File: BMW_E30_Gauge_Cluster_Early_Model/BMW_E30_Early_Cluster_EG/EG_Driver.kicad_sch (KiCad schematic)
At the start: 23 parts, among them Q2 BC337, U1 4049, U4 LM2903, U5 SAJ300R, U6 PIC1655A, Y1 160 kHz

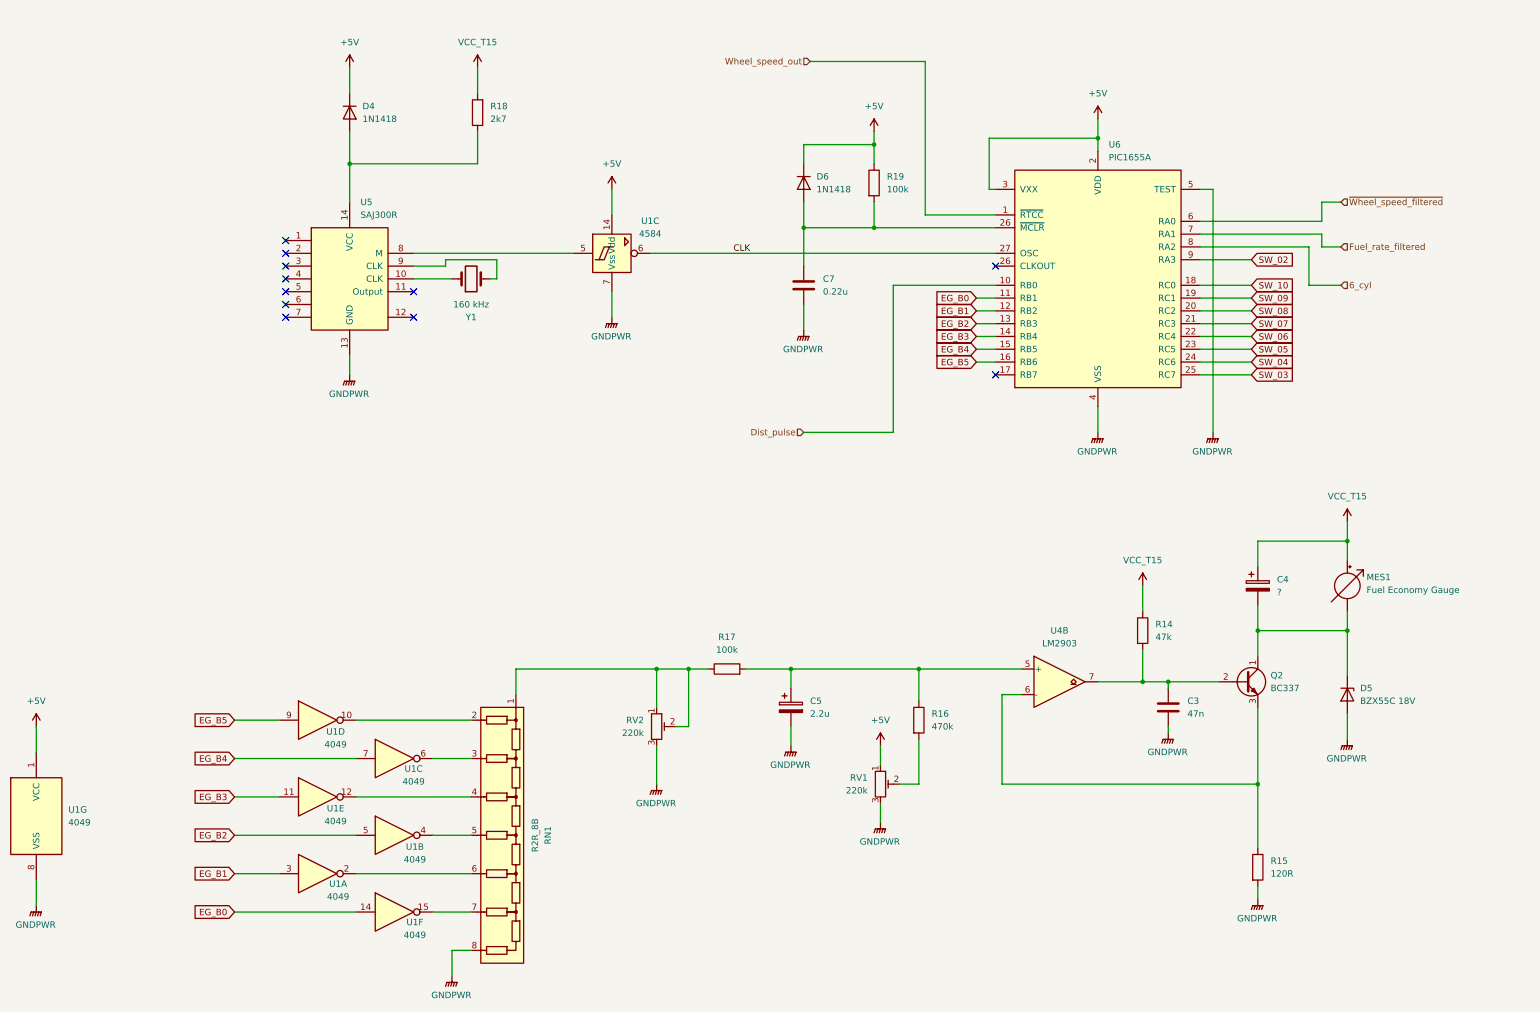
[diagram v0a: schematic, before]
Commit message: Layout Updates for EG
TODO: fix reference designators that were rewritten by accident. Original reference designators are listed in the schematic pdf.
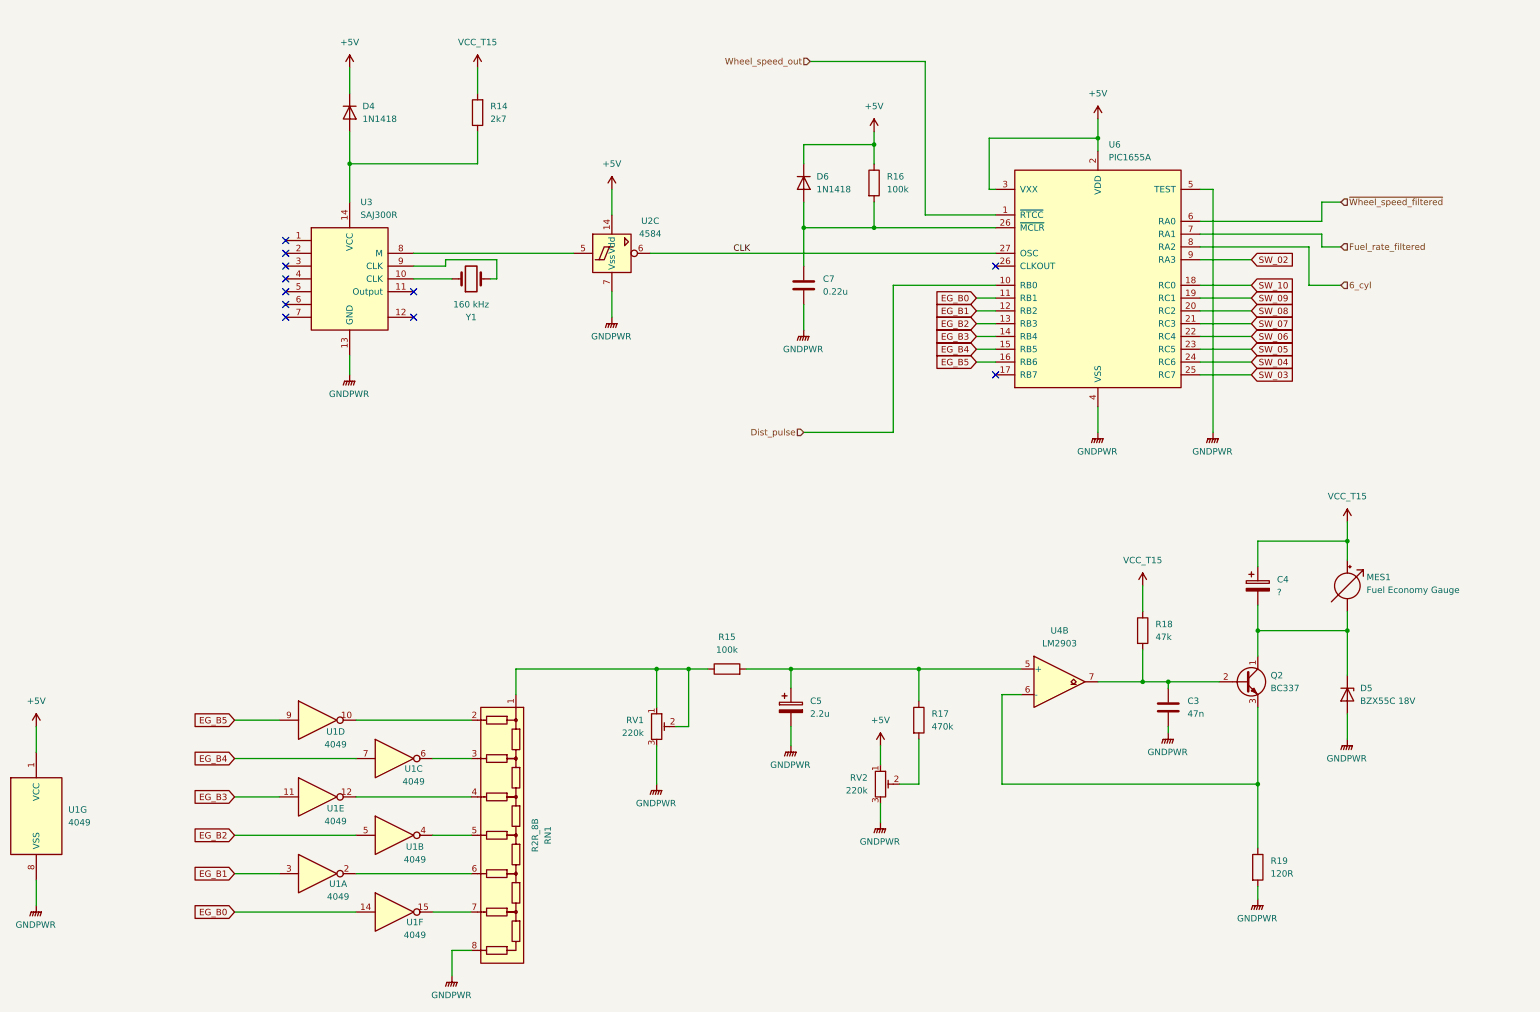
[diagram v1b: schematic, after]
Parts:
- Q2: footprint Package_TO_SOT_THT:TO-92_Inline -> Package_TO_SOT_THT:TO-92L_Wide
- RV1: renamed from RV2; footprint (none) -> Potentiometer_THT:Potentiometer_ACP_CA9-H2,5_Horizontal
- RV2: renamed from RV1; footprint (none) -> Potentiometer_THT:Potentiometer_ACP_CA9-H2,5_Horizontal
- U1: footprint Package_DIP:DIP-16_W7.62mm -> Package_DIP:DIP-16_W7.62mm_Socket_LongPads
- U3: renamed from U5; footprint (none) -> Package_DIP:DIP-14_W7.62mm_Socket_LongPads
- U6: footprint Package_DIP:DIP-28_W15.24mm -> Package_DIP:DIP-28_W15.24mm_Socket_LongPads
- Y1: footprint (none) -> Crystal:Crystal_HC49-U_Vertical
- renumbered R18 to R14, R17 to R15, R19 to R16, R16 to R17, R14 to R18, R15 to R19, U1 to U2
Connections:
- net at U6.26 (CLKOUT): now also C7.1, D6.2 (A), R16.2

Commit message: EG Layout Updates
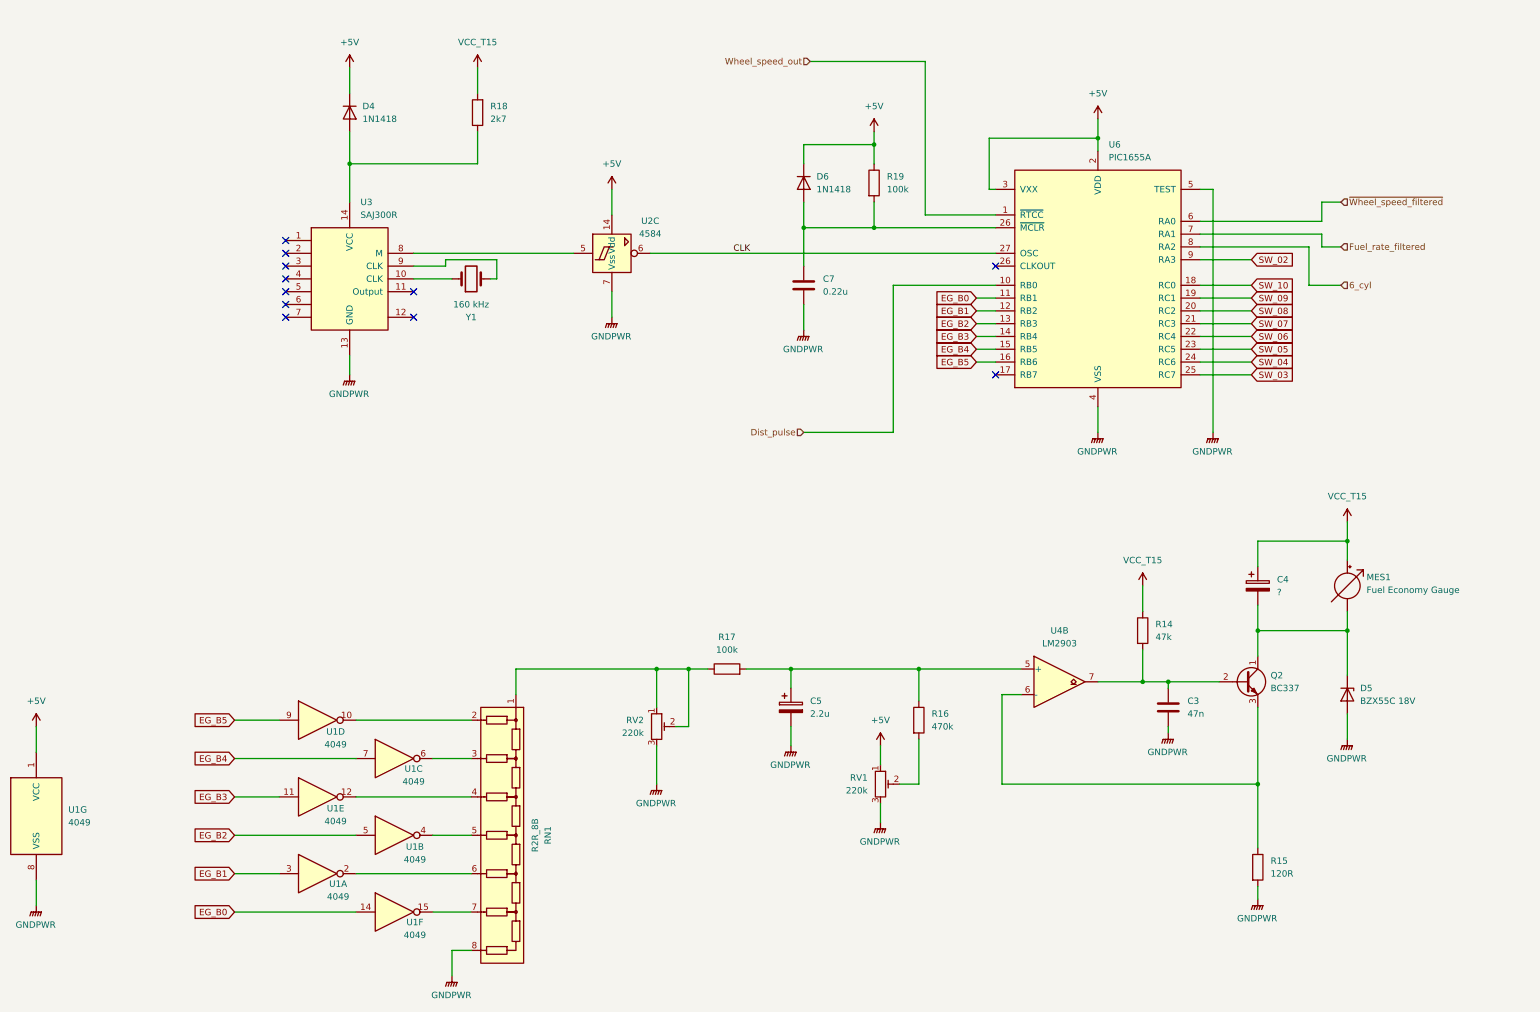
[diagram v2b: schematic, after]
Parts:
- renumbered R18 to R14, R19 to R15, R17 to R16, R15 to R17, R14 to R18, R16 to R19, RV2 to RV1, RV1 to RV2
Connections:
- net at U6.26 (CLKOUT): now also C7.1, D6.2 (A), R19.2
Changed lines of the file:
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@@
 		(dnp no)
 		(fields_autoplaced yes)
-		(property "Reference" "R17"
+		(property "Reference" "R16"
 			(at 236.22 173.9899 0)
 			(effects
@@
 			(project "BMW_E30_Early_Cluster_EG"
 				(path "/b216cb44-2546-4a52-a541-225697d17737/523a037d-2c6e-49de-a758-40f01dbf4536"
-					(reference "R17")
+					(reference "R16")
 					(unit 1)
 				)
@@
 		(dnp no)
 		(fields_autoplaced yes)
-		(property "Reference" "R18"
+		(property "Reference" "R14"
 			(at 280.67 156.2099 0)
 			(effects
@@
 			(project "BMW_E30_Early_Cluster_EG"
 				(path "/b216cb44-2546-4a52-a541-225697d17737/523a037d-2c6e-49de-a758-40f01dbf4536"
-					(reference "R18")
+					(reference "R14")
 					(unit 1)
 				)
@@
 		(dnp no)
 		(fields_autoplaced yes)
-		(property "Reference" "R16"
+		(property "Reference" "R19"
 			(at 227.33 67.3099 0)
 			(effects
@@
 			(project "BMW_E30_Early_Cluster_EG"
 				(path "/b216cb44-2546-4a52-a541-225697d17737/523a037d-2c6e-49de-a758-40f01dbf4536"
-					(reference "R16")
+					(reference "R19")
 					(unit 1)
 				)
@@
 		(dnp no)
 		(fields_autoplaced yes)
-		(property "Reference" "R15"
+		(property "Reference" "R17"
 			(at 195.58 158.75 90)
 			(effects
@@
 			(project "BMW_E30_Early_Cluster_EG"
 				(path "/b216cb44-2546-4a52-a541-225697d17737/523a037d-2c6e-49de-a758-40f01dbf4536"
-					(reference "R15")
+					(reference "R17")
 					(unit 1)
 				)
@@
 		(dnp no)
 		(fields_autoplaced yes)
-		(property "Reference" "R14"
+		(property "Reference" "R18"
 			(at 148.59 53.3399 0)
 			(effects
@@
 			(project "BMW_E30_Early_Cluster_EG"
 				(path "/b216cb44-2546-4a52-a541-225697d17737/523a037d-2c6e-49de-a758-40f01dbf4536"
-					(reference "R14")
+					(reference "R18")
 					(unit 1)
 				)
@@
 		(dnp no)
 		(fields_autoplaced yes)
-		(property "Reference" "RV1"
+		(property "Reference" "RV2"
 			(at 179.07 175.2599 0)
 			(effects
@@
 			(project "BMW_E30_Early_Cluster_EG"
 				(path "/b216cb44-2546-4a52-a541-225697d17737/523a037d-2c6e-49de-a758-40f01dbf4536"
-					(reference "RV1")
+					(reference "RV2")
 					(unit 1)
 				)
@@
 		(dnp no)
 		(fields_autoplaced yes)
-		(property "Reference" "RV2"
+		(property "Reference" "RV1"
 			(at 223.52 186.6899 0)
 			(effects
@@
 			(project "BMW_E30_Early_Cluster_EG"
 				(path "/b216cb44-2546-4a52-a541-225697d17737/523a037d-2c6e-49de-a758-40f01dbf4536"
-					(reference "RV2")
+					(reference "RV1")
 					(unit 1)
 				)
@@
 		(dnp no)
 		(fields_autoplaced yes)
-		(property "Reference" "R19"
+		(property "Reference" "R15"
 			(at 303.53 203.1999 0)
 			(effects
@@
 			(project "BMW_E30_Early_Cluster_EG"
 				(path "/b216cb44-2546-4a52-a541-225697d17737/523a037d-2c6e-49de-a758-40f01dbf4536"
-					(reference "R19")
+					(reference "R15")
 					(unit 1)
 				)

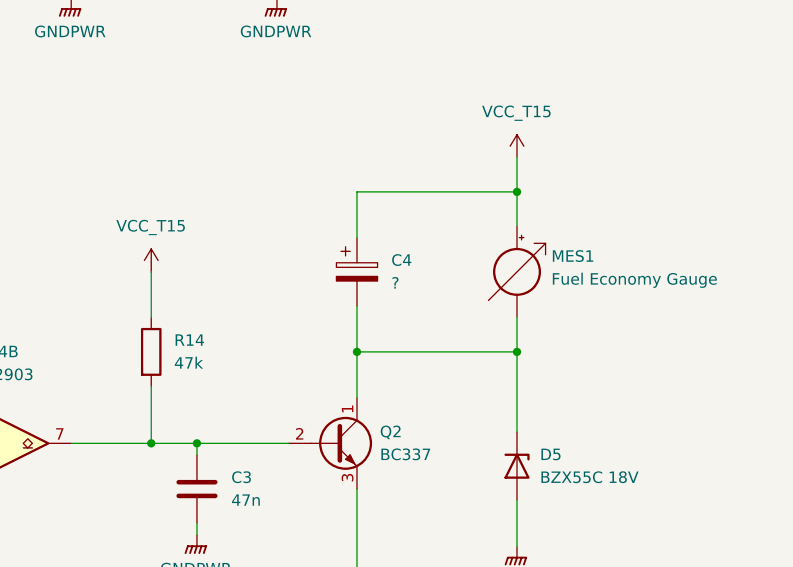
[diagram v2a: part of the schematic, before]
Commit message: EG Layout Updates
Added capacitor footprints and moved all resistors into place.
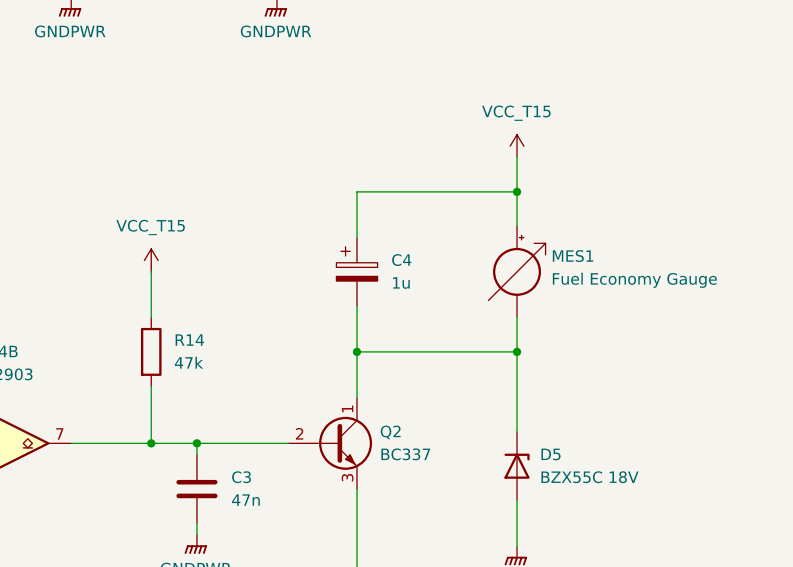
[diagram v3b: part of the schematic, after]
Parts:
- C3: footprint (none) -> Capacitor_THT:C_Rect_L11.5mm_W3.6mm_P10.00mm_MKT
- C4: value ? -> 1u; footprint (none) -> Capacitor_THT:CP_Radial_Tantal_D5.0mm_P2.50mm
- C5: footprint (none) -> Capacitor_THT:CP_Radial_Tantal_D4.5mm_P2.50mm
- C7: footprint (none) -> Capacitor_THT:C_Rect_L10.0mm_W3.0mm_P7.50mm_FKS3_FKP3
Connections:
- net at U6.26 (CLKOUT): now also C7.1, D6.2 (A), R19.2
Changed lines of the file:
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@@
 			)
 		)
-		(property "Value" "?"
+		(property "Value" "1u"
 			(at 304.8 149.8599 0)
 			(effects
@@
 			)
 		)
-		(property "Footprint" ""
+		(property "Footprint" "Capacitor_THT:CP_Radial_Tantal_D5.0mm_P2.50mm"
 			(at 301.9552 152.4 0)
 			(effects
@@
 			)
 		)
-		(property "Footprint" ""
+		(property "Footprint" "Capacitor_THT:C_Rect_L10.0mm_W3.0mm_P7.50mm_FKS3_FKP3"
 			(at 211.7852 92.71 0)
 			(effects
@@
 			)
 		)
-		(property "Footprint" ""
+		(property "Footprint" "Capacitor_THT:CP_Radial_Tantal_D4.5mm_P2.50mm"
 			(at 209.2452 176.53 0)
 			(effects
@@
 			)
 		)
-		(property "Footprint" ""
+		(property "Footprint" "Capacitor_THT:C_Rect_L11.5mm_W3.6mm_P10.00mm_MKT"
 			(at 284.1752 176.53 0)
 			(effects
